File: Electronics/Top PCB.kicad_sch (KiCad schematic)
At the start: 1 part

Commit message: made some changes
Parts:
- added PiServo1, PiServo2: Conn_01x03_Male, Connector_PinHeader_2.54mm:PinHeader_1x03_P2.54mm_Vertical, symbol Connector:Conn_01x03_Male
- renumbered Servo1 to PenServo1
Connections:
- net +5V: now also PiServo1.2 (Pin_2), PiServo2.2 (Pin_2)
- net GND: now also PiServo1.1 (Pin_1), PiServo2.1 (Pin_1)
- new net RPi/PiServo1: PiServo1.3 (Pin_3)
- new net RPi/PiServo2: PiServo2.3 (Pin_3)
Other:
- sheet RPi ports: added PiServo1, PiServo2; removed none
- moved on the sheet: PenServo1

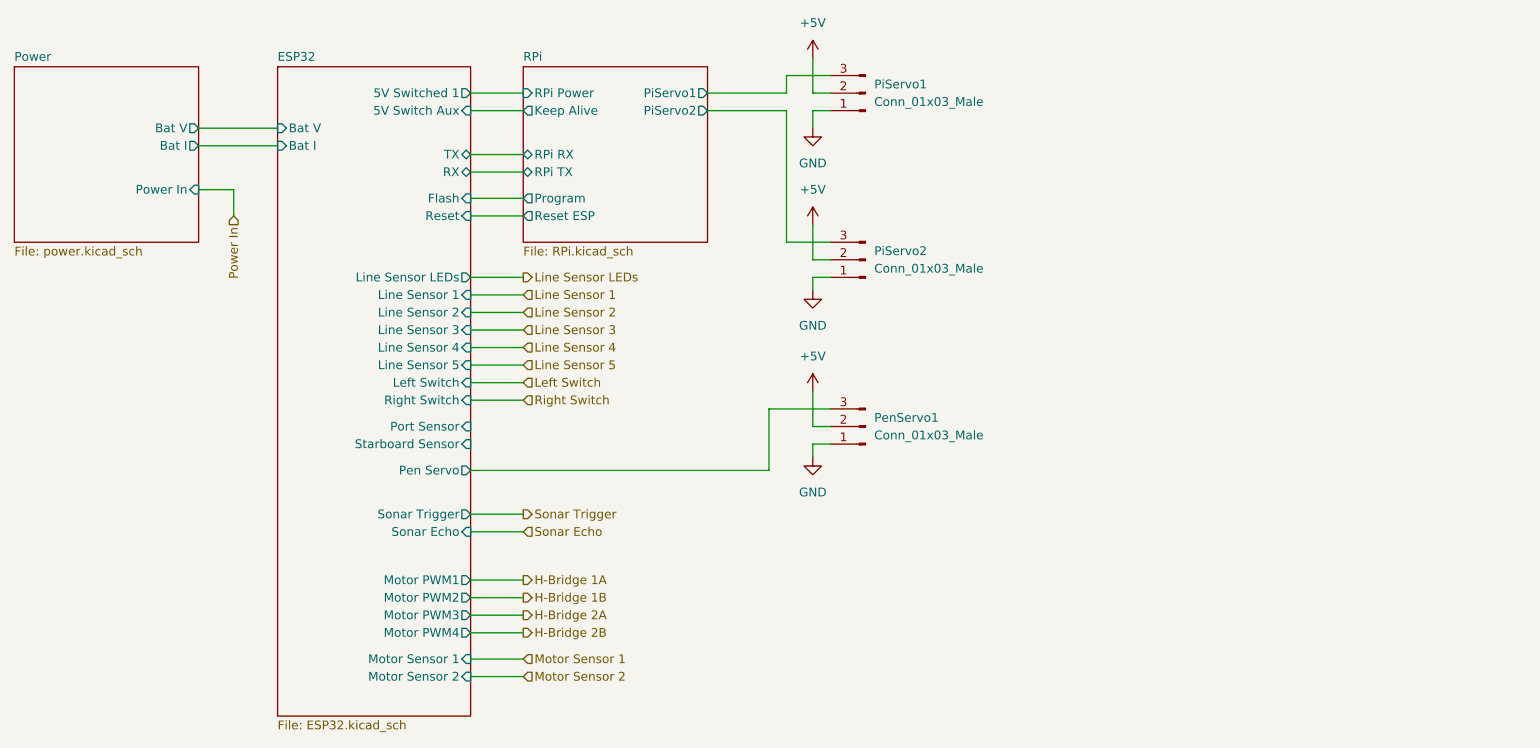
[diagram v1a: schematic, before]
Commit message: added bom
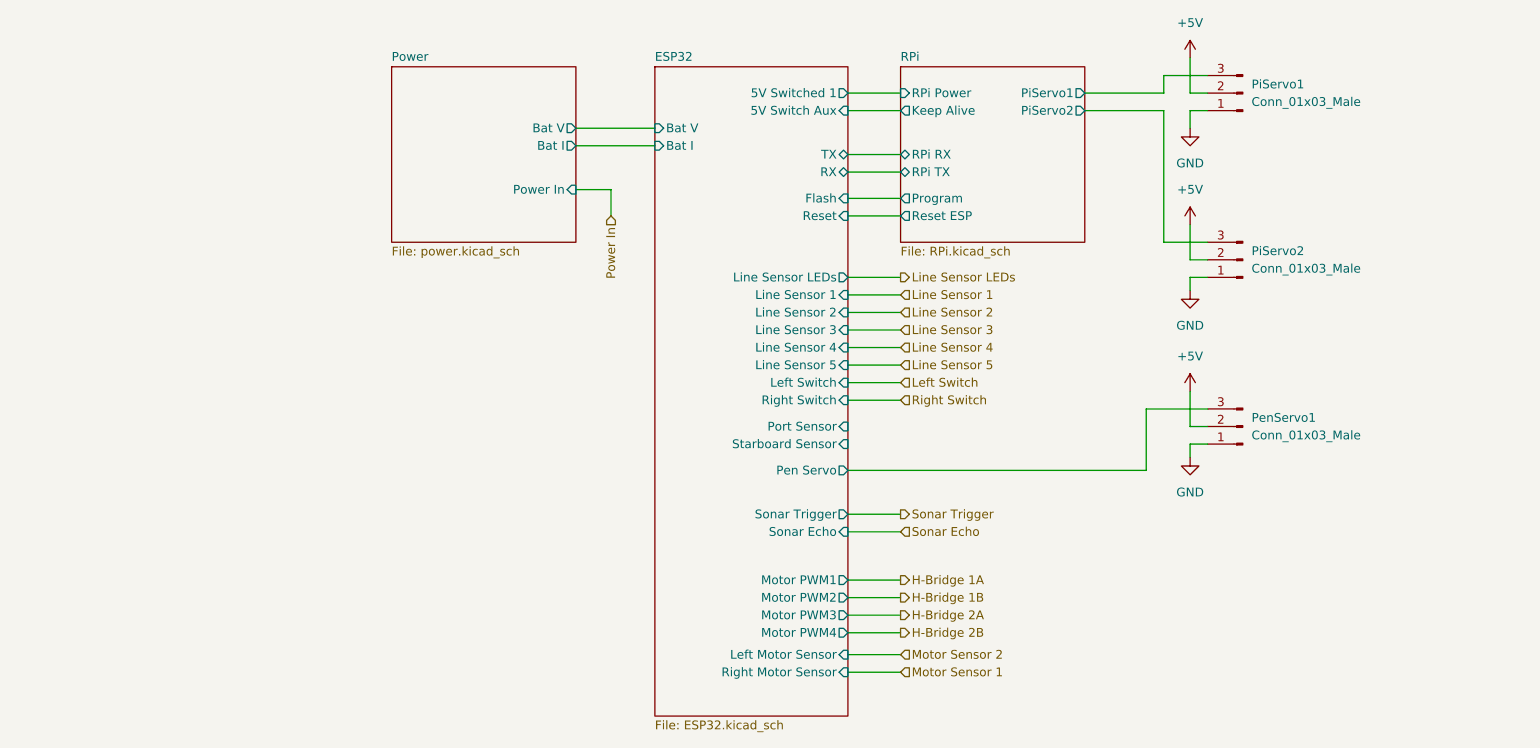
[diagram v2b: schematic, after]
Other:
- sheet ESP32 ports: added Left Motor Sensor, Right Motor Sensor; removed Motor Sensor 1, Motor Sensor 2
- moved on the sheet: PenServo1, PiServo1, PiServo2

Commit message: yep
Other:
- moved on the sheet: PenServo1, PiServo1, PiServo2

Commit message: some changes were made
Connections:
- net ESP32/Pen Servo renamed Pen Servo
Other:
- sheet ESP32 ports: added Bottom PCB V; removed Port Sensor, Starboard Sensor
- company: (none) -> Squashed Fly
- title: (none) -> Swarmbot
- moved on the sheet: PenServo1
